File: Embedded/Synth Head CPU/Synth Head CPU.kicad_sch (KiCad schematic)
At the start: 24 parts, among them J1 10171746-00021LF, J2 JST [C], J3 MSD-1-A, J4 JST [N], Q1 BSS138, U5 FFC [G], U6 FFC [M], U7 FFC [K], U9 SRV05-4

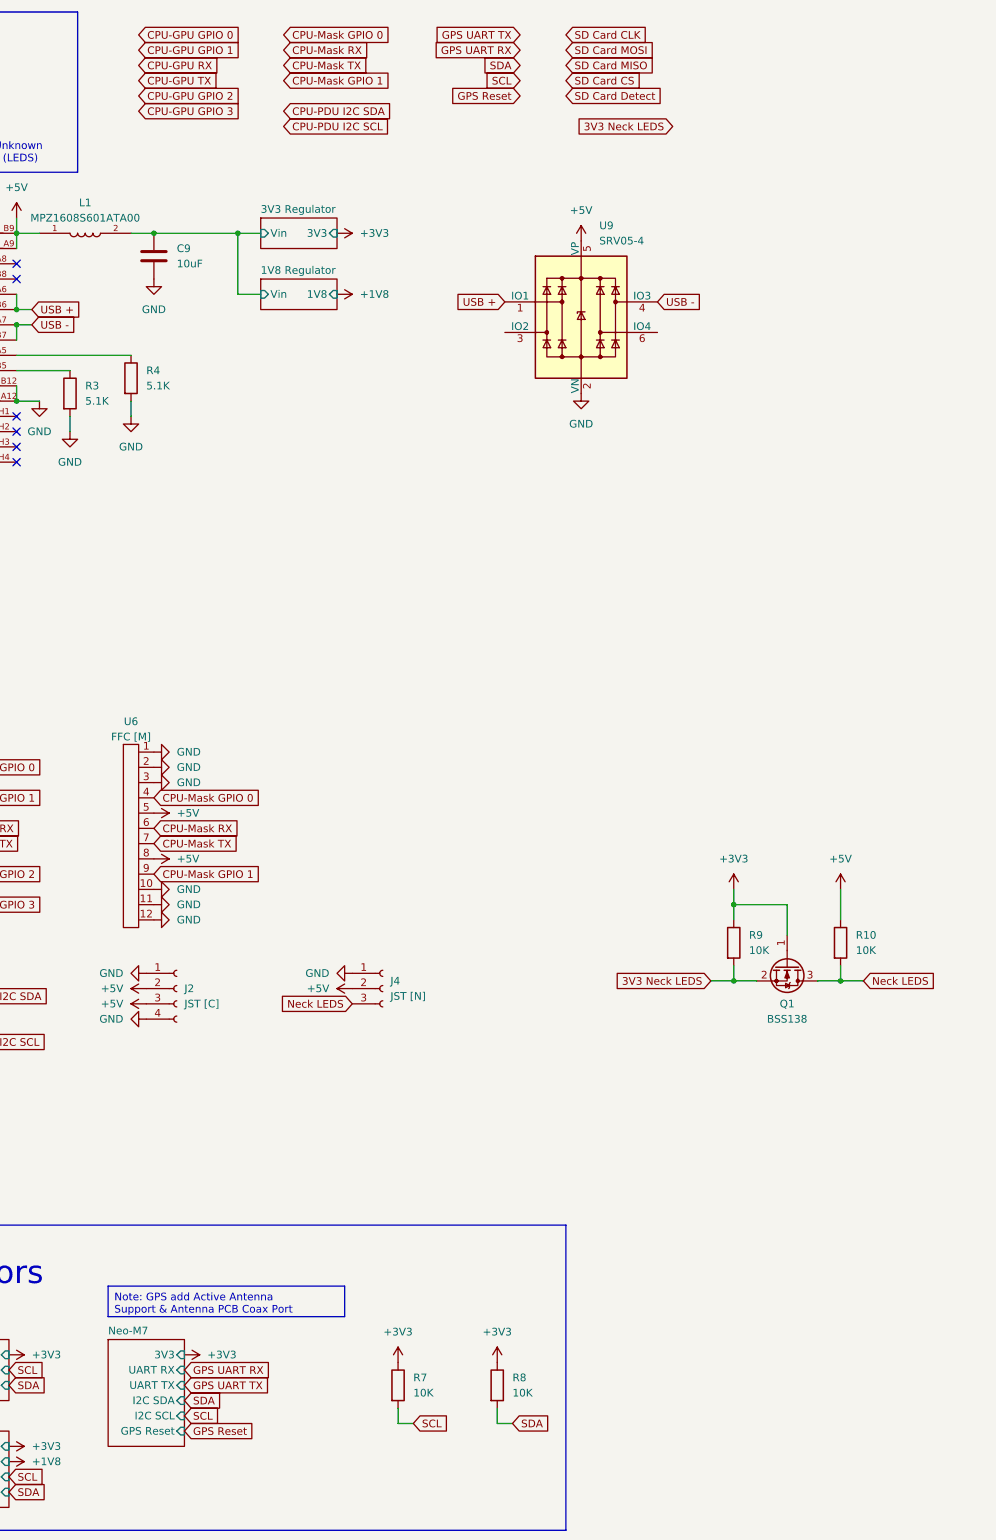
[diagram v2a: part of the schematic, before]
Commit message: Added GPS RF Port
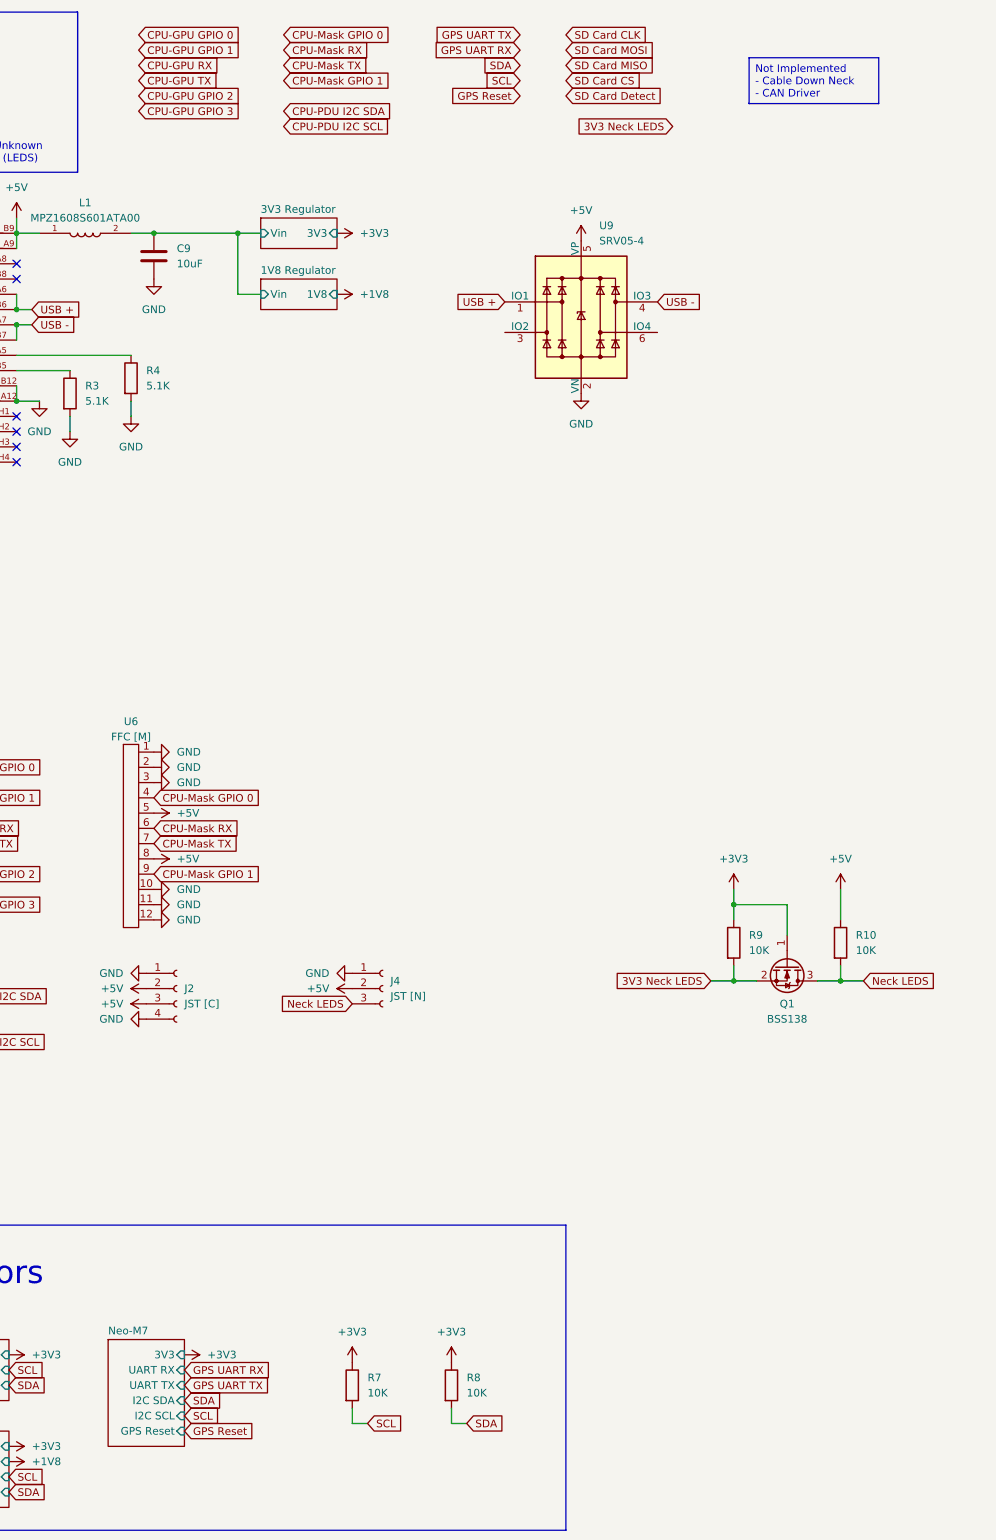
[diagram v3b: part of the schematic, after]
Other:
- moved on the sheet: R7, R8
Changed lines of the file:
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@@
 	(wire
 		(pts
-			(xy 106.68 252.73) (xy 106.68 250.19)
+			(xy 99.06 252.73) (xy 99.06 250.19)
 		)
 		(stroke
@@
 	(wire
 		(pts
-			(xy 125.73 252.73) (xy 123.19 252.73)
+			(xy 118.11 252.73) (xy 115.57 252.73)
 		)
 		(stroke
@@
 	(wire
 		(pts
-			(xy 106.68 252.73) (xy 109.22 252.73)
+			(xy 99.06 252.73) (xy 101.6 252.73)
 		)
 		(stroke
@@
 	(wire
 		(pts
-			(xy 123.19 252.73) (xy 123.19 250.19)
+			(xy 115.57 252.73) (xy 115.57 250.19)
 		)
 		(stroke
@@
 		)
 	)
-	(text_box "Note: GPS add Active Antenna Support & Antenna PCB Coax Port"
+	(text_box "Not Implemented\n- Cable Down Neck\n- CAN Driver"
 		(exclude_from_sim no)
-		(at 58.42 229.87 0)
-		(size 39.37 5.08)
+		(at 165.1 25.4 0)
+		(size 21.59 7.62)
 		(stroke
 			(width 0)
@@
 	(global_label "SDA"
 		(shape input)
-		(at 125.73 252.73 0)
+		(at 118.11 252.73 0)
 		(fields_autoplaced yes)
 		(effects
@@
 		)
 		(property "Intersheetrefs" "${INTERSHEET_REFS}"
-			(at 132.2833 252.73 0)
+			(at 124.6633 252.73 0)
 			(effects
 				(font
@@
 	(global_label "SCL"
 		(shape input)
-		(at 109.22 252.73 0)
+		(at 101.6 252.73 0)
 		(fields_autoplaced yes)
 		(effects
@@
 		)
 		(property "Intersheetrefs" "${INTERSHEET_REFS}"
-			(at 115.7128 252.73 0)
+			(at 108.0928 252.73 0)
 			(effects
 				(font
@@
 	(symbol
 		(lib_id "Device:R")
-		(at 106.68 246.38 0)
+		(at 99.06 246.38 0)
 		(unit 1)
 		(exclude_from_sim no)
@@
 		(fields_autoplaced yes)
 		(property "Reference" "R7"
-			(at 109.22 245.1099 0)
+			(at 101.6 245.1099 0)
 			(effects
 				(font
@@
 		)
 		(property "Value" "10K"
-			(at 109.22 247.6499 0)
+			(at 101.6 247.6499 0)
 			(effects
 				(font
@@
 		)
 		(property "Footprint" ""
-			(at 104.902 246.38 90)
+			(at 97.282 246.38 90)
 			(effects
 				(font
@@
 		)
 		(property "Datasheet" "~"
-			(at 106.68 246.38 0)
+			(at 99.06 246.38 0)
 			(effects
 				(font
@@
 		)
 		(property "Description" "Resistor"
-			(at 106.68 246.38 0)
+			(at 99.06 246.38 0)
 			(effects
 				(font
@@
 	(symbol
 		(lib_id "power:+3V3")
-		(at 106.68 242.57 0)
+		(at 99.06 242.57 0)
 		(unit 1)
 		(exclude_from_sim no)
@@
 		(fields_autoplaced yes)
 		(property "Reference" "#PWR067"
-			(at 106.68 246.38 0)
+			(at 99.06 246.38 0)
 			(effects
 				(font
@@
 		)
 		(property "Value" "+3V3"
-			(at 106.68 237.49 0)
+			(at 99.06 237.49 0)
 			(effects
 				(font
@@
 		)
 		(property "Footprint" ""
-			(at 106.68 242.57 0)
+			(at 99.06 242.57 0)
 			(effects
 				(font
@@
 		)
 		(property "Datasheet" ""
-			(at 106.68 242.57 0)
+			(at 99.06 242.57 0)
 			(effects
 				(font
@@
 		)
 		(property "Description" "Power symbol creates a global label with name \"+3V3\""
-			(at 106.68 242.57 0)
+			(at 99.06 242.57 0)
 			(effects
 				(font
@@
 	(symbol
 		(lib_id "Device:R")
-		(at 123.19 246.38 0)
+		(at 115.57 246.38 0)
 		(unit 1)
 		(exclude_from_sim no)
@@
 		(fields_autoplaced yes)
 		(property "Reference" "R8"
-			(at 125.73 245.1099 0)
+			(at 118.11 245.1099 0)
 			(effects
 				(font
@@
 		)
 		(property "Value" "10K"
-			(at 125.73 247.6499 0)
+			(at 118.11 247.6499 0)
 			(effects
 				(font
@@
 		)
 		(property "Footprint" ""
-			(at 121.412 246.38 90)
+			(at 113.792 246.38 90)
 			(effects
 				(font
@@
 		)
 		(property "Datasheet" "~"
-			(at 123.19 246.38 0)
+			(at 115.57 246.38 0)
 			(effects
 				(font
@@
 		)
 		(property "Description" "Resistor"
-			(at 123.19 246.38 0)
+			(at 115.57 246.38 0)
 			(effects
 				(font
@@
 	(symbol
 		(lib_id "power:+3V3")
-		(at 123.19 242.57 0)
+		(at 115.57 242.57 0)
 		(unit 1)
 		(exclude_from_sim no)
@@
 		(fields_autoplaced yes)
 		(property "Reference" "#PWR068"
-			(at 123.19 246.38 0)
+			(at 115.57 246.38 0)
 			(effects
 				(font
@@
 		)
 		(property "Value" "+3V3"
-			(at 123.19 237.49 0)
+			(at 115.57 237.49 0)
 			(effects
 				(font
@@
 		)
 		(property "Footprint" ""
-			(at 123.19 242.57 0)
+			(at 115.57 242.57 0)
 			(effects
 				(font
@@
 		)
 		(property "Datasheet" ""
-			(at 123.19 242.57 0)
+			(at 115.57 242.57 0)
 			(effects
 				(font
@@
 		)
 		(property "Description" "Power symbol creates a global label with name \"+3V3\""
-			(at 123.19 242.57 0)
+			(at 115.57 242.57 0)
 			(effects
 				(font

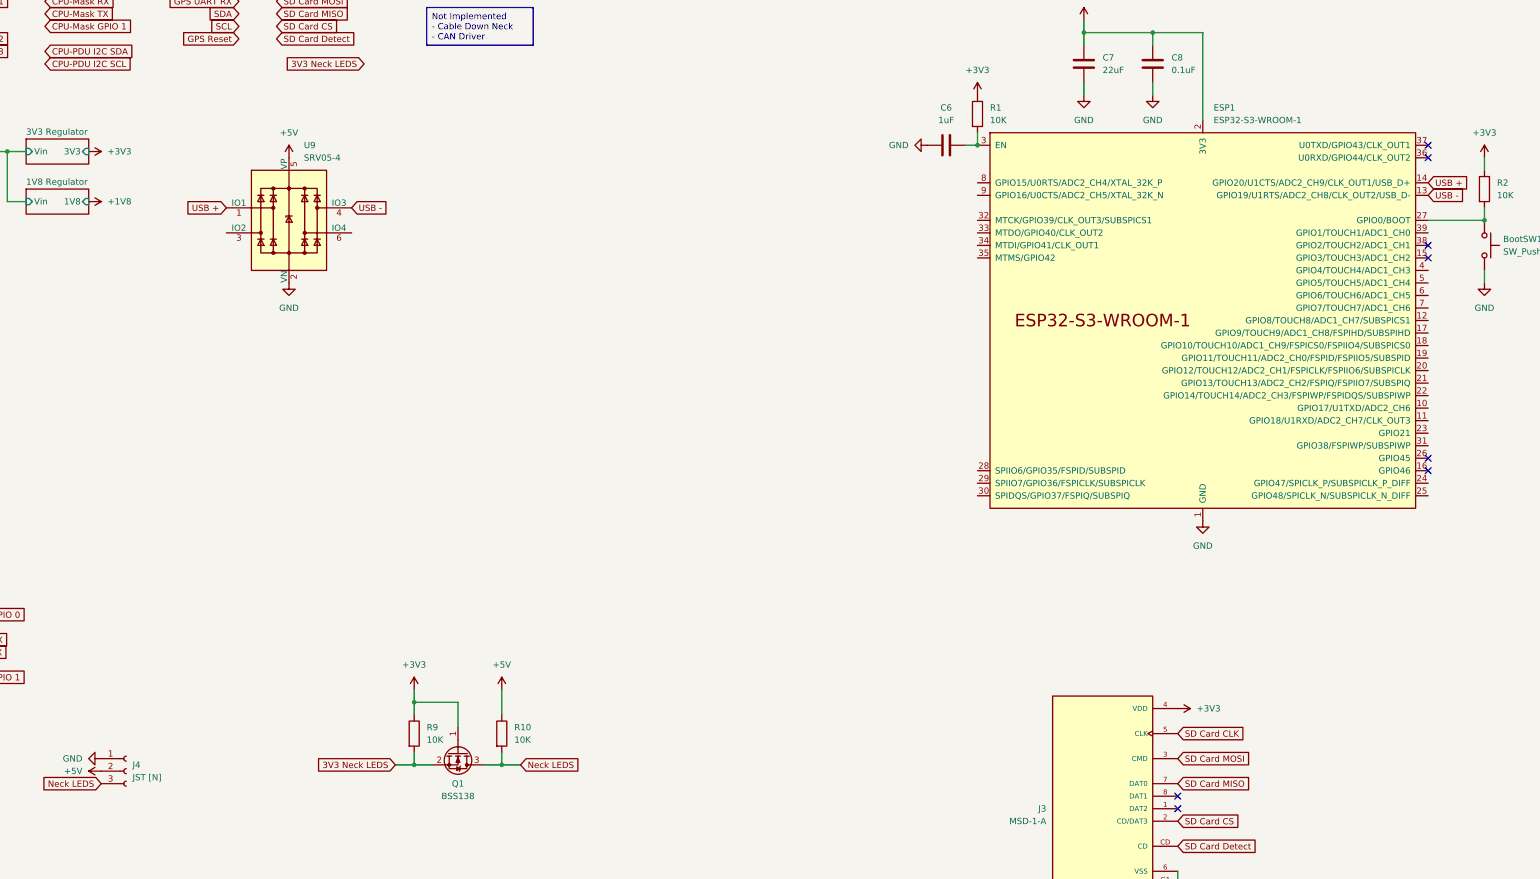
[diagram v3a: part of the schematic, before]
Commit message: Added Power Indicator LEDS & Decoupling Caps
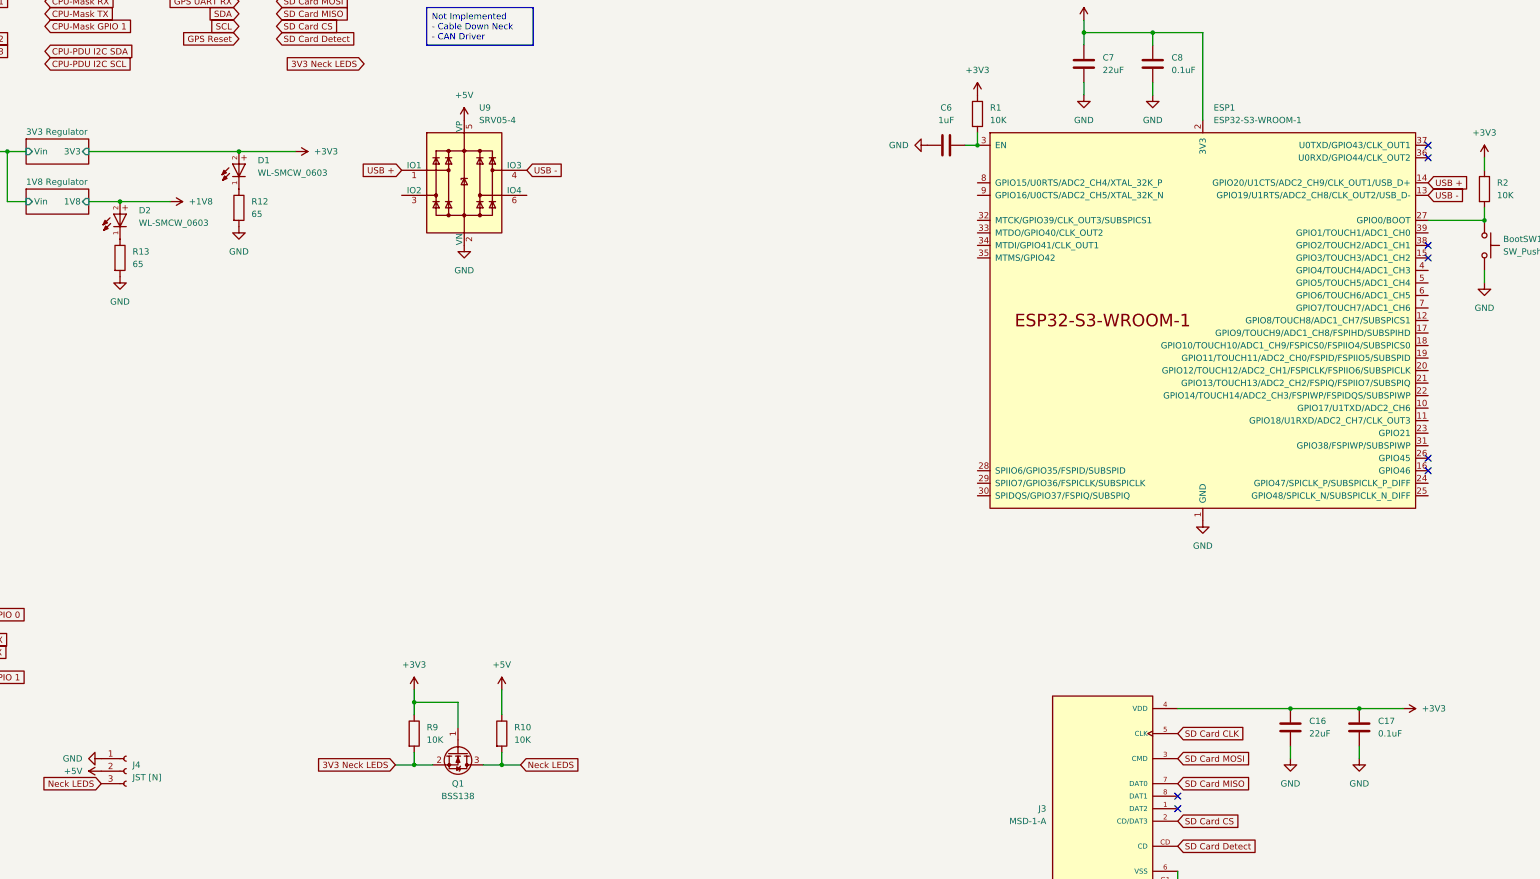
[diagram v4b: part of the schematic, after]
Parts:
- added C16: 22uF, Capacitor_SMD:C_0603_1608Metric_Pad1.08x0.95mm_HandSolder, symbol Device:C
- added C17: 0.1uF, Capacitor_SMD:C_0603_1608Metric, symbol Device:C
- added D1, D2: WL-SMCW_0603, LED_Red_SMD:WL-SMCW_0603, symbol LED_Red_SMD:WL-SMCW_0603
- added R12, R13: 65, symbol Device:R
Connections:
- net +1V8: now also D2.2
- net +3V3: now also C16.1, C17.1, D1.2
- net GND: now also C16.2, C17.2, R12.2, R13.2
- new net: D2.1, R13.1
- new net: D1.1, R12.1
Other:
- moved on the sheet: U9

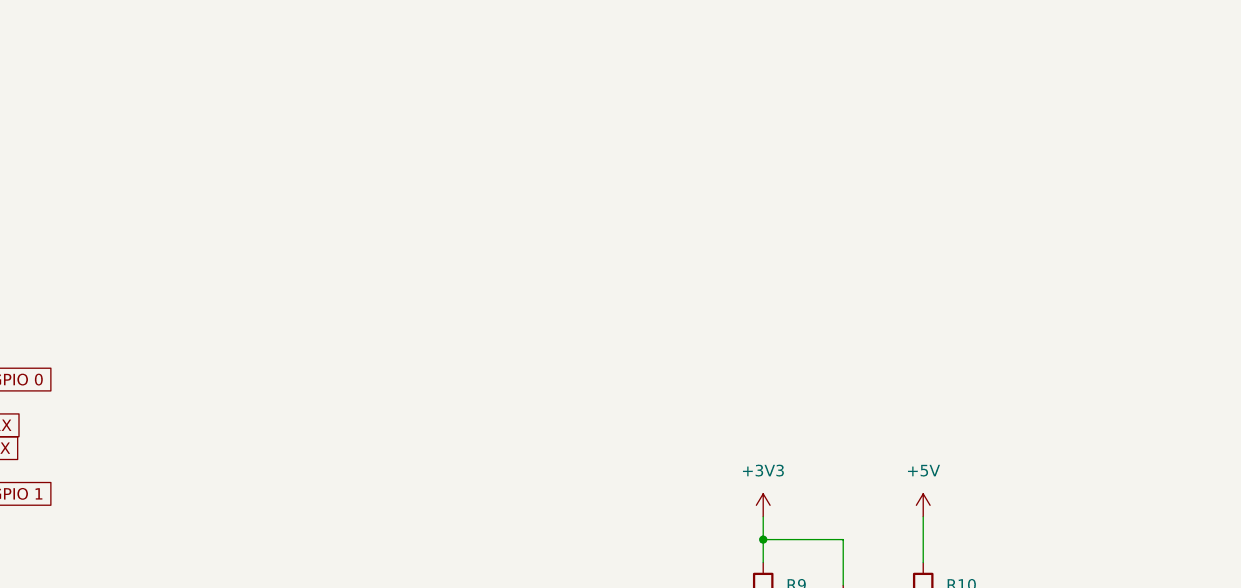
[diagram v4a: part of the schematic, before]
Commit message: Added Jaw LEDS
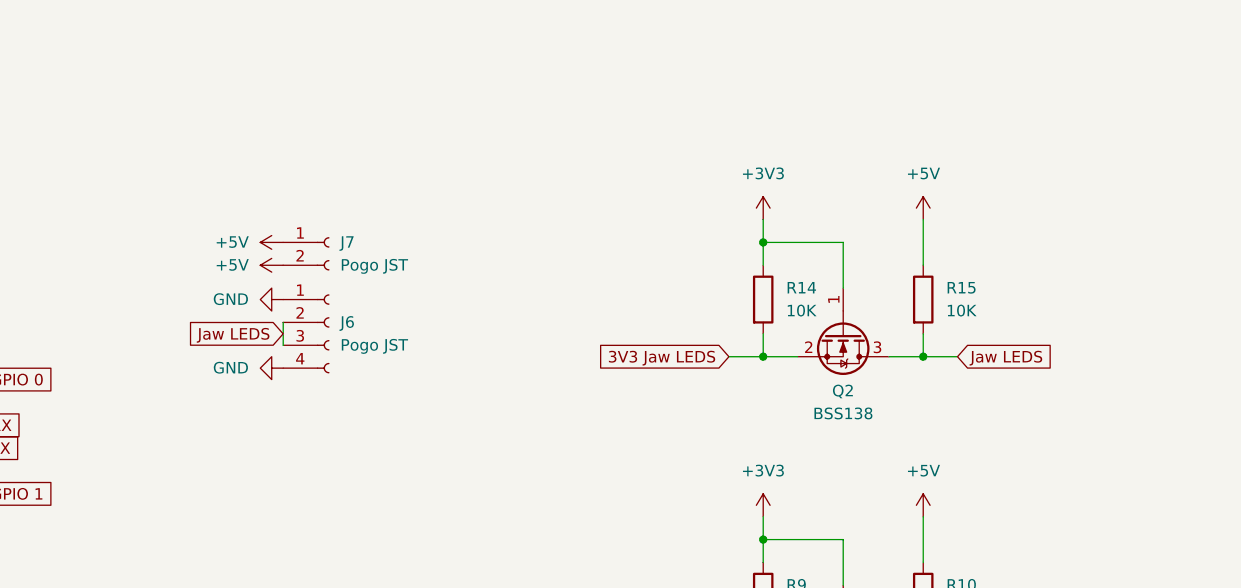
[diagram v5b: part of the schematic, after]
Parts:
- added J6: Pogo JST, symbol Connector:Conn_01x04_Socket
- added J7: Pogo JST, symbol Connector:Conn_01x02_Socket
- added Q2: BSS138, Package_TO_SOT_SMD:SOT-23, symbol Transistor_FET:BSS138
- added R14, R15: 10K, symbol Device:R
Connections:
- net +3V3: now also Q2.1 (G), R14.1
- net +5V: now also J7.1 (Pin_1), J7.2 (Pin_2), R15.1
- net GND: now also J6.1 (Pin_1), J6.4 (Pin_4)
- new net 3V3 Jaw LEDS: Q2.2 (S), R14.2
- new net Jaw LEDS: J6.2 (Pin_2), J6.3 (Pin_3), Q2.3 (D), R15.2

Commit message: Prepared All Main Boards for PCB Creation
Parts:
- C17, C8: footprint Capacitor_SMD:C_0603_1608Metric -> Capacitor_SMD:C_0603_1608Metric_Pad1.08x0.95mm_HandSolder
- J2, J6: footprint (none) -> Connector_Molex:Molex_PicoBlade_53048-0410_1x04_P1.25mm_Horizontal
- J3: footprint MSD-1-A:CUI_MSD-1-A -> MicroSD_MSD_1_A:CUI_MSD-1-A
- J4: footprint (none) -> Connector_Molex:Molex_PicoBlade_53048-0310_1x03_P1.25mm_Horizontal
- J7: footprint (none) -> Connector_Molex:Molex_PicoBlade_53048-0210_1x02_P1.25mm_Horizontal
- R10, R12, R13, R14, R15, R7, R8, R9: footprint (none) -> Resistor_SMD:R_0603_1608Metric_Pad0.98x0.95mm_HandSolder
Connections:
- net +5V: no longer U7.3, U7.4
- net USB +: now also U7.3
- net USB -: now also U7.4
- net CPU-PDU I2C SCL renamed CPU-PDU SCL
- net CPU-PDU I2C SDA renamed CPU-PDU SDA
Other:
- moved on the sheet: J2
